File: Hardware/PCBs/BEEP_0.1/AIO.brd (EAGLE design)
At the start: 106 x 69.1 mm, 80 parts, among them IC1 ULN2803ASOP18, IC2 ULN2803ASOP18, IC3 74HC238D, IC4 74HC238D, U2 TB6612FNG, U3 ATXMEGA64D3-AU, X10 MICROMATCH-10, X3 MICROMATCH-8, X4 MICROMATCH-8, X5 MICROMATCH-8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

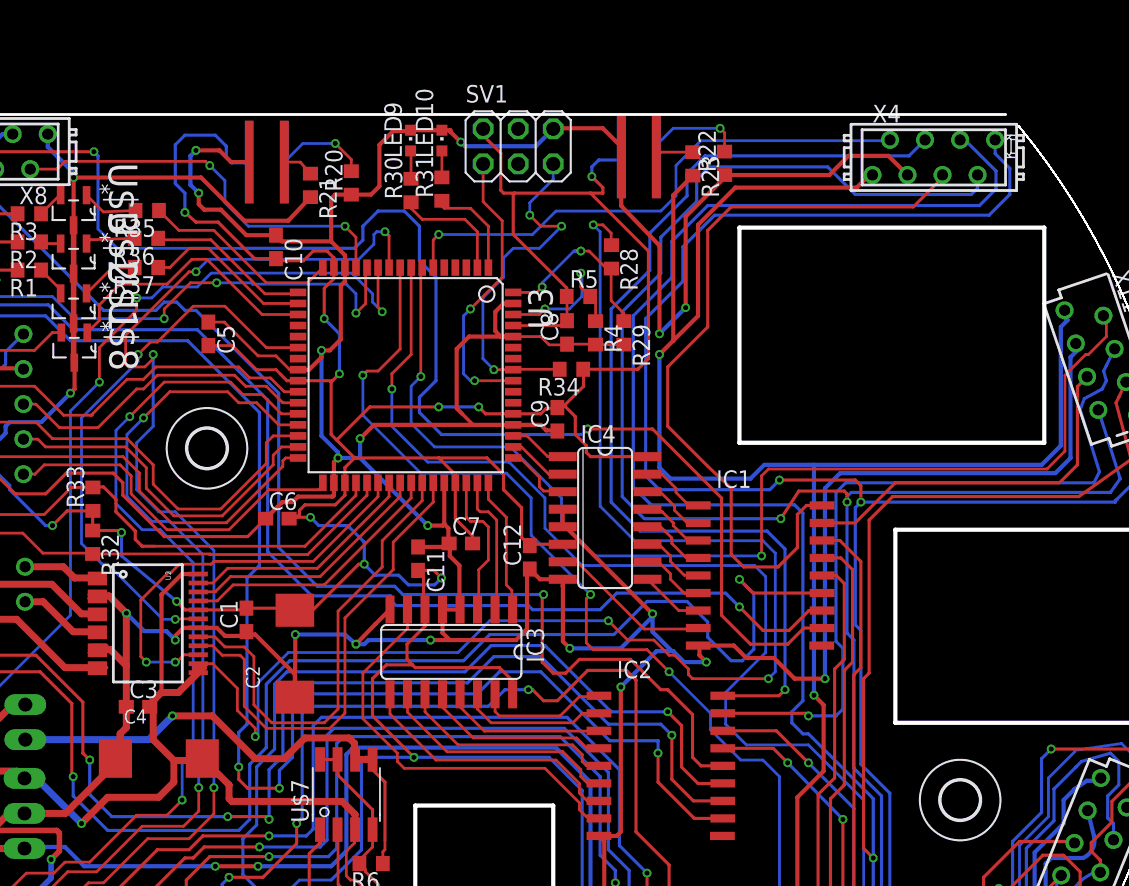
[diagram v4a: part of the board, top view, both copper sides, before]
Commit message: continue routing replace so16 multiplexer with ssop16 add ssop16 footprint to beep library
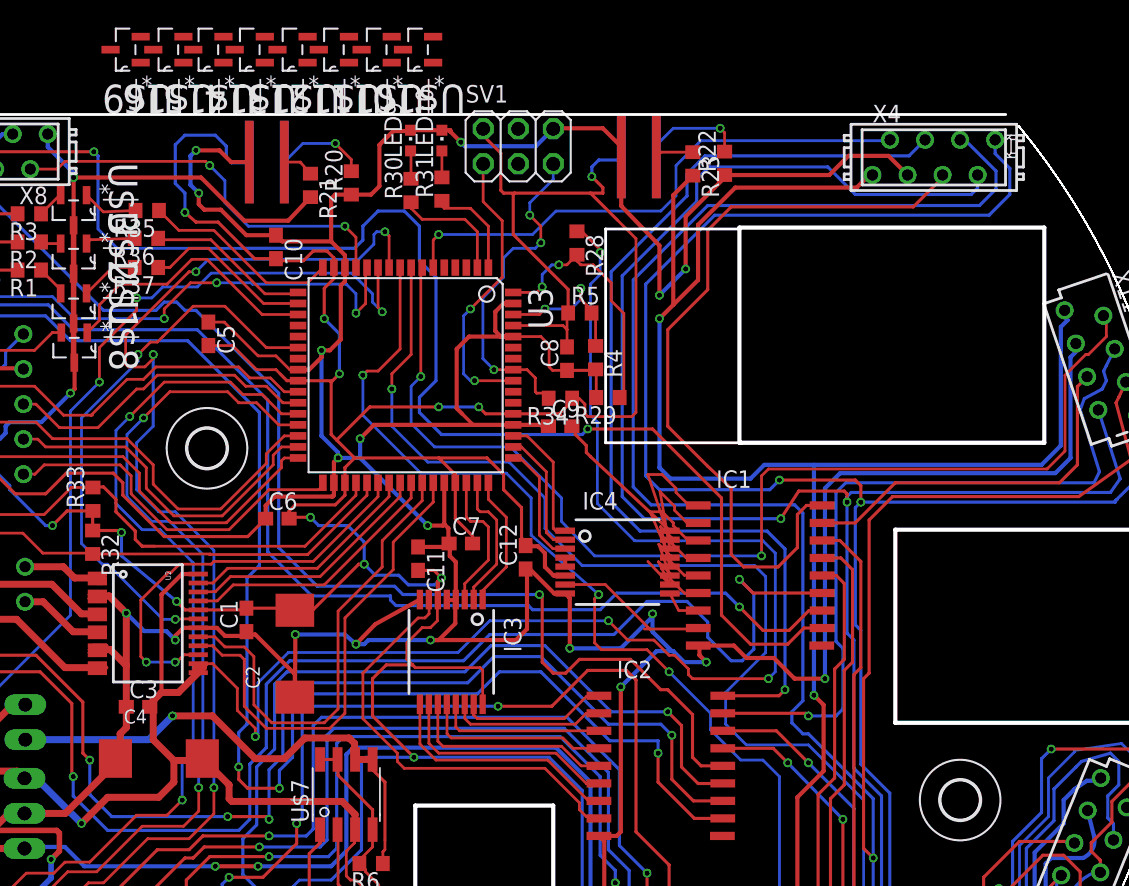
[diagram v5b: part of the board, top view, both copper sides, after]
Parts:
- added U$10, U$11, U$12, U$13, U$14, U$15, U$16, U$9: DMN2075U, BEEP:SOT95P240X112-3N
- IC3, IC4: value 74HC238D -> 74HC238SSOP; device BEEP:SO16 -> BEEP:SSOP16
- moved R29 4.83 mm to (61.0, 54.3), turned to 180 degrees
- moved IC4 3.32 mm to (61.7, 42.4)
- moved R28 2.69 mm to (58.7, 65.5)
- moved R34 2.25 mm to (57.5, 54.2)
- moved C8 1.90 mm to (58.0, 57.1)
- moved R4 1.80 mm to (60.1, 57.2)
- moved R5 1.20 mm to (58.9, 60.4)
- moved C9 0.54 mm to (57.5, 52.2), turned to 0 degrees
- moved C12 0.30 mm to (55.0, 42.7)
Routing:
- net GND: track 600.5 -> 589.3 mm
- net +3V3: track 352.2 -> 360.5 mm
- net RGB_LED_MK0: track 4.21 -> 9.45 mm
- net N$21: track 4.85 -> 9.80 mm
- net RGB_LED_MK1: track 4.43 -> 9.13 mm
- net BATT_VOLTAGE: track 14.1 -> 18.7 mm
- net RGB_LED_MK2: track 5.01 -> 8.95 mm
- net N$27: track 4.74 -> 8.10 mm
- net N$31: track 4.90 -> 8.23 mm
- net N$24: track 4.80 -> 8.07 mm
- net +5V: track 398.4 -> 395.8 mm
- net N$12: track 19.6 -> 17.6 mm
- net N$28: track 4.85 -> 6.87 mm
- net N$33: track 4.62 -> 2.81 mm
- net +7V: track 171.1 -> 169.3 mm
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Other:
- outline, holes or cut-outs redrawn

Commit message: continue routing...
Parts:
- moved C9 5.76 mm to (55.8, 46.7), turned to 270 degrees
- moved C12 5.35 mm to (53.4, 37.6)
- moved R34 5.00 mm to (58.7, 49.4), turned to 90 degrees
- moved IC3 4.55 mm to (50.7, 31.4), turned to 270 degrees
- moved IC4 2.56 mm to (59.7, 40.8)
- moved R29 2.36 mm to (58.7, 53.7), turned to 90 degrees
- moved C7 1.42 mm to (49.4, 42.6), turned to 90 degrees
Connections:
- net IR_LED_MK0: now also U3.46; no longer U3.48
- net IR_LED_MK2: now also U3.48; no longer U3.46
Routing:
- net +3V3: track 360.5 -> 379.7 mm
- net +7V: track 169.3 -> 188.0 mm
- net GND: track 589.3 -> 607.2 mm
- net N$13: track 31.7 -> 16.4 mm
- net IR_LED_K0_OUT: track 73.3 -> 87.3 mm
- net N$12: track 17.6 -> 7.97 mm
- net N$10: track 16.4 -> 7.78 mm
- net IR_LED_MK2: track 10.4 -> 18.9 mm
- net N$9: track 15.1 -> 7.04 mm
- net IR_LED_MK1: track 10.1 -> 17.8 mm
- net IR_LED_MK0: track 9.78 -> 16.7 mm
- net N$7: track 13.6 -> 6.79 mm
- net LED_K4_OUT: track 132.2 -> 126.2 mm
- net N$6: track 12.1 -> 6.55 mm
- net N$34: track 11.4 -> 17.0 mm
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
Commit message: Add audio amplifier correct batt rev circuit and on off circuit some routing
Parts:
- removed U$10, U$11, U$12, U$13, U$14, U$15, U$16, U$9: DMN2075U, BEEP:SOT95P240X112-3N
- added IC5: TS34119SMD, BEEP:SO08
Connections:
- net +5V: now also IC5.6
- net +7V: now also U$7.5, U$7.6; no longer R41.1, U$7.3
- net BATT_GND: no longer U$5.S
- net BATT_U: now also R41.1, U$7.3; no longer U$7.5, U$7.6
- net GND: now also IC5.7, U$5.S; no longer U$5.D
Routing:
- net +7V: track 188.0 -> 183.3 mm
- net GND: track 607.2 -> 602.9 mm
- net BATT_U: track 37.1 -> 38.0 mm
- net BATT_GND: track 18.5 -> 17.8 mm
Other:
- board size 106 x 69.1 mm -> 106.2 x 69.1 mm
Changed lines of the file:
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@@
 <wire x1="90.729890625" y1="6.61673125" x2="90.729890625" y2="73.98326875" width="0.001" layer="20" curve="78.919109"/>
 <wire x1="9.5" y1="74.8" x2="89.8" y2="74.8" width="0.2032" layer="20"/>
-<wire x1="9.5" y1="5.7" x2="48.5" y2="5.7" width="0.2032" layer="20"/>
-<wire x1="48.5" y1="5.7" x2="55.3" y2="5.7" width="0.2032" layer="20"/>
-<wire x1="55.3" y1="5.7" x2="90.2" y2="5.7" width="0.2032" layer="20"/>
-<wire x1="70.5" y1="66.6" x2="92.6" y2="66.6" width="0.3048" layer="20"/>
-<wire x1="92.6" y1="66.6" x2="92.6" y2="51" width="0.3048" layer="20"/>
-<wire x1="92.6" y1="51" x2="70.6" y2="51" width="0.3048" layer="20"/>
-<wire x1="70.6" y1="51" x2="70.5" y2="51" width="0.3048" layer="20"/>
-<wire x1="70.5" y1="51" x2="70.5" y2="66.5" width="0.3048" layer="20"/>
-<wire x1="70.5" y1="66.5" x2="70.5" y2="66.6" width="0.3048" layer="20"/>
-<wire x1="81.8" y1="44.7" x2="99.2" y2="44.7" width="0.3048" layer="20"/>
-<wire x1="99.2" y1="44.7" x2="99.2" y2="30.7" width="0.3048" layer="20"/>
-<wire x1="99.2" y1="30.7" x2="81.8" y2="30.7" width="0.3048" layer="20"/>
-<wire x1="81.8" y1="30.7" x2="81.8" y2="44.7" width="0.3048" layer="20"/>
-<wire x1="47" y1="24.7" x2="57" y2="24.7" width="0.3048" layer="20"/>
-<wire x1="57" y1="24.7" x2="57" y2="14.6" width="0.3048" layer="20"/>
-<wire x1="57" y1="14.6" x2="55.3" y2="14.6" width="0.3048" layer="20"/>
-<wire x1="55.3" y1="14.6" x2="55.3" y2="5.7" width="0.3048" layer="20"/>
-<wire x1="48.5" y1="5.7" x2="48.5" y2="14.6" width="0.3048" layer="20"/>
-<wire x1="48.5" y1="14.6" x2="47" y2="14.6" width="0.3048" layer="20"/>
-<wire x1="47" y1="14.6" x2="47" y2="24.7" width="0.3048" layer="20"/>
-<wire x1="70.6" y1="51" x2="60.8" y2="51" width="0.2032" layer="20"/>
-<wire x1="60.8" y1="51" x2="60.8" y2="66.5" width="0.2032" layer="20"/>
-<wire x1="70.5" y1="66.5" x2="60.8" y2="66.5" width="0.2032" layer="20"/>
+<wire x1="9.5" y1="5.7" x2="90.2" y2="5.7" width="0.2032" layer="20"/>
+<wire x1="81.165" y1="45.335" x2="103.01" y2="45.335" width="0.3048" layer="20"/>
+<wire x1="103.01" y1="30.065" x2="81.165" y2="30.065" width="0.3048" layer="20"/>
+<wire x1="81.165" y1="30.065" x2="81.165" y2="45.335" width="0.3048" layer="20"/>
 </plain>
 <attributes>
@@
 <attribute name="OC_FARNELL" value="176432" x="-8.5" y="9.5" size="1.778" layer="27" display="off"/>
 </element>
-<element name="U$9" library="BEEP" package="SOT95P240X112-3N" value="DMN2075U" x="26" y="79.5" rot="R180"/>
-<element name="U$10" library="BEEP" package="SOT95P240X112-3N" value="DMN2075U" x="47.2" y="79.5" rot="R180"/>
-<element name="U$11" library="BEEP" package="SOT95P240X112-3N" value="DMN2075U" x="44.2" y="79.5" rot="R180"/>
-<element name="U$12" library="BEEP" package="SOT95P240X112-3N" value="DMN2075U" x="41.1" y="79.5" rot="R180"/>
-<element name="U$13" library="BEEP" package="SOT95P240X112-3N" value="DMN2075U" x="38.1" y="79.5" rot="R180"/>
-<element name="U$14" library="BEEP" package="SOT95P240X112-3N" value="DMN2075U" x="35" y="79.5" rot="R180"/>
-<element name="U$15" library="BEEP" package="SOT95P240X112-3N" value="DMN2075U" x="32" y="79.5" rot="R180"/>
-<element name="U$16" library="BEEP" package="SOT95P240X112-3N" value="DMN2075U" x="29.1" y="79.5" rot="R180"/>
+<element name="IC5" library="BEEP" package="SO08" value="TS34119SMD" x="-18.4" y="7.4"/>
 </elements>
 <signals>
@@
 <contactref element="IC1" pad="9"/>
 <contactref element="IC1" pad="9"/>
-<contactref element="U$5" pad="D"/>
 <contactref element="JP12" pad="2"/>
-<contactref element="R42" pad="2"/>
 <contactref element="IC2" pad="9"/>
 <contactref element="IC2" pad="9"/>
@@
 <wire x1="25.26" y1="28.11" x2="25.46" y2="27.96" width="0.508" layer="1"/>
 <wire x1="25.46" y1="27.96" x2="21.63" y2="24.13" width="0.508" layer="1"/>
-<wire x1="11.9522" y1="23.02" x2="14.02" y2="23.02" width="0.508" layer="1"/>
-<wire x1="14.02" y1="23.02" x2="14.31" y2="22.73" width="0.508" layer="1"/>
-<wire x1="14.31" y1="22.73" x2="16.13" y2="22.73" width="0.508" layer="1"/>
 <wire x1="16.13" y1="22.73" x2="16.4" y2="23" width="0.508" layer="1"/>
 <wire x1="16.4" y1="23" x2="17.6" y2="24.2" width="0.508" layer="1"/>
@@
 <wire x1="5.419384375" y1="20.919384375" x2="7.5" y2="23" width="0.3048" layer="1"/>
 <wire x1="7.5" y1="23" x2="11.9322" y2="23" width="0.3048" layer="1"/>
-<wire x1="11.9322" y1="23" x2="11.9522" y2="23.02" width="0.3048" layer="1"/>
 <wire x1="17.245" y1="9.92" x2="17.145" y2="11.345" width="0.3048" layer="16"/>
 <wire x1="17.145" y1="11.345" x2="18.7" y2="12.9" width="0.3048" layer="16"/>
@@
 <wire x1="55.8" y1="48.1" x2="56.8" y2="49.1" width="0.2032" layer="1"/>
 <wire x1="56.8" y1="49.1" x2="56.8" y2="50.6" width="0.2032" layer="1"/>
+<contactref element="U$5" pad="S"/>
+<contactref element="R42" pad="2"/>
+<contactref element="IC5" pad="7"/>
 <wire x1="31.5" y1="13.5" x2="36.5" y2="13" width="0" layer="19" extent="1-1"/>
 <wire x1="24.072" y1="15.304" x2="30.4" y2="12.4" width="0" layer="19" extent="1-1"/>
 <wire x1="19" y1="17.1" x2="24.072" y2="15.304" width="0" layer="19" extent="1-1"/>
+<wire x1="14.31" y1="22.73" x2="16.13" y2="22.73" width="0" layer="19" extent="1-1"/>
+<wire x1="11.9322" y1="23" x2="14.31" y2="22.73" width="0" layer="19" extent="1-1"/>
+<wire x1="9.7678" y1="22.0802" x2="11.9322" y2="23" width="0" layer="19" extent="1-1"/>
+<wire x1="-19.035" y1="9.9432" x2="3.474903125" y2="20.919384375" width="0" layer="19" extent="1-1"/>
 </signal>
 <signal name="LED_K4_OUT">
@@
 <wire x1="62.9" y1="13.9" x2="59.9" y2="16.9" width="0.3048" layer="16"/>
 <wire x1="62.9" y1="13.9" x2="68.1" y2="13.9" width="0.3048" layer="16"/>
+<contactref element="IC5" pad="6"/>
+<wire x1="-17.765" y1="9.9432" x2="3.46410625" y2="20.38060625" width="0" layer="19" extent="1-1"/>
 </signal>
 <signal name="+3V3">
@@
 <contactref element="R28" pad="1"/>
 <contactref element="JP12" pad="1"/>
-<contactref element="R41" pad="1"/>
-<contactref element="LED11" pad="A"/>
 <wire x1="27.75" y1="31.86" x2="27.95" y2="32.25" width="0.508" layer="1"/>
 <wire x1="27.95" y1="32.25" x2="28.6" y2="32.9" width="0.508" layer="1"/>
@@
 <wire x1="28.4" y1="25.3" x2="29.5" y2="26.4" width="0.508" layer="1"/>
 <wire x1="29.5" y1="26.4" x2="29.5" y2="27.97" width="0.508" layer="1"/>
-<wire x1="7.13" y1="25.76" x2="9.36" y2="25.76" width="0.508" layer="1"/>
-<wire x1="9.36" y1="25.76" x2="9.77" y2="26.17" width="0.508" layer="1"/>
-<wire x1="9.77" y1="26.17" x2="9.77" y2="26.87" width="0.508" layer="1"/>
 <wire x1="9.77" y1="26.87" x2="10.1" y2="27.2" width="0.508" layer="1"/>
 <wire x1="10.1" y1="27.2" x2="18.14" y2="27.2" width="0.508" layer="1"/>
@@
 <wire x1="37.8" y1="35.8" x2="35.6" y2="33.6" width="0.2032" layer="16"/>
 <contactref element="R8" pad="1"/>
-<contactref element="U$7" pad="3"/>
-<wire x1="42.635" y1="22.9568" x2="42.635" y2="24.065" width="0.508" layer="1"/>
 <wire x1="42.635" y1="24.065" x2="41.7" y2="25" width="0.508" layer="1"/>
 <wire x1="18.14" y1="27.2" x2="18.67" y2="26.67" width="0.508" layer="1"/>
@@
 <wire x1="42" y1="21.4" x2="42.6" y2="22" width="0.2032" layer="1"/>
 <wire x1="42.6" y1="22" x2="42.6" y2="22.9218" width="0.2032" layer="1"/>
-<wire x1="42.6" y1="22.9218" x2="42.635" y2="22.9568" width="0.2032" layer="1"/>
 <wire x1="32.1" y1="28.1" x2="31.57" y2="28.1" width="0.508" layer="1"/>
 <wire x1="31.57" y1="28.1" x2="31.56" y2="28.11" width="0.508" layer="1"/>
@@
 <wire x1="56.8" y1="66.3" x2="58.69" y2="66.3" width="0.2032" layer="1"/>
 <wire x1="58.69" y1="66.3" x2="58.72" y2="66.33" width="0.2032" layer="1"/>
+<contactref element="U$7" pad="5"/>
+<contactref element="U$7" pad="6"/>
+<contactref element="LED11" pad="A"/>
+<wire x1="42.635" y1="28.0432" x2="43.905" y2="28.0432" width="0" layer="19" extent="1-1"/>
+<wire x1="41.7" y1="25" x2="42.635" y2="28.0432" width="0" layer="19" extent="1-1"/>
+<wire x1="9.77" y1="26.17" x2="9.77" y2="26.87" width="0" layer="19" extent="1-1"/>
+<wire x1="42.6" y1="22.9218" x2="42.635" y2="24.065" width="0" layer="19" extent="1-1"/>
 </signal>
 <signal name="MOTOR_STBY">
@@
 </signal>
 <signal name="BATT_GND">
-<contactref element="U$5" pad="S"/>
 <contactref element="JP13" pad="2"/>
-<wire x1="9.7678" y1="22.0802" x2="10.5198" y2="22.0802" width="0.508" layer="1"/>
 <wire x1="10.5198" y1="22.0802" x2="11.5" y2="21.1" width="0.508" layer="1"/>
 <via x="11.5" y="21.1" extent="1-16" drill="0.3556" shape="octagon"/>
@@
 <contactref element="JP13" pad="1"/>
 <contactref element="R6" pad="1"/>
-<contactref element="U$7" pad="5"/>
-<contactref element="U$7" pad="6"/>
 <wire x1="44.8" y1="22.2" x2="44.8" y2="26.4" width="0.2286" layer="1"/>
 <wire x1="44.8" y1="26.4" x2="43.9" y2="27.3" width="0.2286" layer="1"/>
 <wire x1="43.9" y1="27.3" x2="43.9" y2="28.0382" width="0.2286" layer="1"/>
-<wire x1="43.9" y1="28.0382" x2="43.905" y2="28.0432" width="0.2286" layer="1"/>
 <wire x1="44.65" y1="20.5" x2="44.65" y2="21.35" width="0.2032" layer="1"/>
 <wire x1="44.65" y1="21.35" x2="44.8" y2="21.5" width="0.2032" layer="1"/>
@@
 <wire x1="42.2" y1="29.6" x2="42.6" y2="29.2" width="0.508" layer="1"/>
 <wire x1="42.6" y1="29.2" x2="42.6" y2="28.0782" width="0.508" layer="1"/>
-<wire x1="42.6" y1="28.0782" x2="42.635" y2="28.0432" width="0.508" layer="1"/>
-<wire x1="42.635" y1="28.0432" x2="43.905" y2="28.0432" width="0.508" layer="1"/>
 <wire x1="32.3" y1="31.2" x2="35.4" y2="28.1" width="0.508" layer="1"/>
+<contactref element="U$7" pad="3"/>
+<contactref element="R41" pad="1"/>
+<wire x1="7.13" y1="25.76" x2="9.36" y2="25.76" width="0.508" layer="1"/>
+<wire x1="42.6" y1="28.0782" x2="43.9" y2="28.0382" width="0" layer="19" extent="1-1"/>
+<wire x1="42.635" y1="22.9568" x2="44.8" y2="22.2" width="0" layer="19" extent="1-1"/>
+<wire x1="9.36" y1="25.76" x2="18.73" y2="29.48" width="0" layer="19" extent="1-1"/>
 </signal>
 </signals>

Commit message: routing
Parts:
- added C14: 100nF, rcl:C0603
- added C15: 1uF, rcl:C0603
- added R10: 3k, rcl:R0603
- added R9: 75k, rcl:R0603
- added X1: MICROMATCH-4, Con-amp-micromatch:MICROMATCH-4
- moved IC5 89.6 mm to (70.5, 18.4), turned to 270 degrees
- moved R34 4.75 mm to (58.0, 54.1)
- moved C9 4.61 mm to (58.8, 50.2), turned to 90 degrees
- moved IC4 2.91 mm to (59.9, 43.6)
- moved R29 1.43 mm to (60.1, 54.0)
- moved LED11 1.27 mm to (11.8, 26.3), turned to 90 degrees
- moved X14 1.12 mm to (3.00, 24.8)
- moved R5 0.94 mm to (58.0, 60.3), turned to 90 degrees
- moved SV1 0.70 mm to (54.5, 71.8)
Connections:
- new net AUDIO_DISABLE: IC5.1
- new net AUDIO_IN: C14.2, X1.3
- new net N$15: IC5.4, R10.1, R9.2
- new net N$17: C14.1, R10.2
- new net N$36: C15.1, IC5.2
- new net SPEAKER_O1: IC5.8, X1.1
- new net SPEAKER_O2: IC5.5, R9.1, X1.2
- net GND: now also C15.2, X1.4
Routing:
- net +7V: track 183.3 -> 171.0 mm
- net GND: track 602.9 -> 610.7 mm
- net +3V3: track 379.7 -> 373.5 mm, vias 15 -> 17
- net LED_K7_OUT: track 101.7 -> 96.2 mm
- net PDI_CLK: track 27.3 -> 22.4 mm
- net N$34: track 17.0 -> 21.3 mm
- net BATT_U: track 38.0 -> 42.1 mm
- net RGB_LED_MK0: track 11.2 -> 7.51 mm
- net RGB_LED_MK2: track 10.4 -> 6.90 mm
- net N$21: track 7.48 -> 4.35 mm
- net N$24: track 6.85 -> 4.09 mm
- net RGB_LED_MK1: track 11.0 -> 8.25 mm
- net BATT_VOLTAGE: track 22.1 -> 19.6 mm, vias 2 -> 0
- net N$27: track 6.12 -> 3.88 mm
- net N$4: track 10.8 -> 9.06 mm, vias 2 -> 0
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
